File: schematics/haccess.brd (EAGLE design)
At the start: 86 x 86 mm, 34 parts, among them Q1 BSS123, SW1 SPST_TACT, SW2 SPST_TACT, U1 MCP2300X/SO, U2 ESP826607B, U3 OPTOISOLATOR-2SOIC8

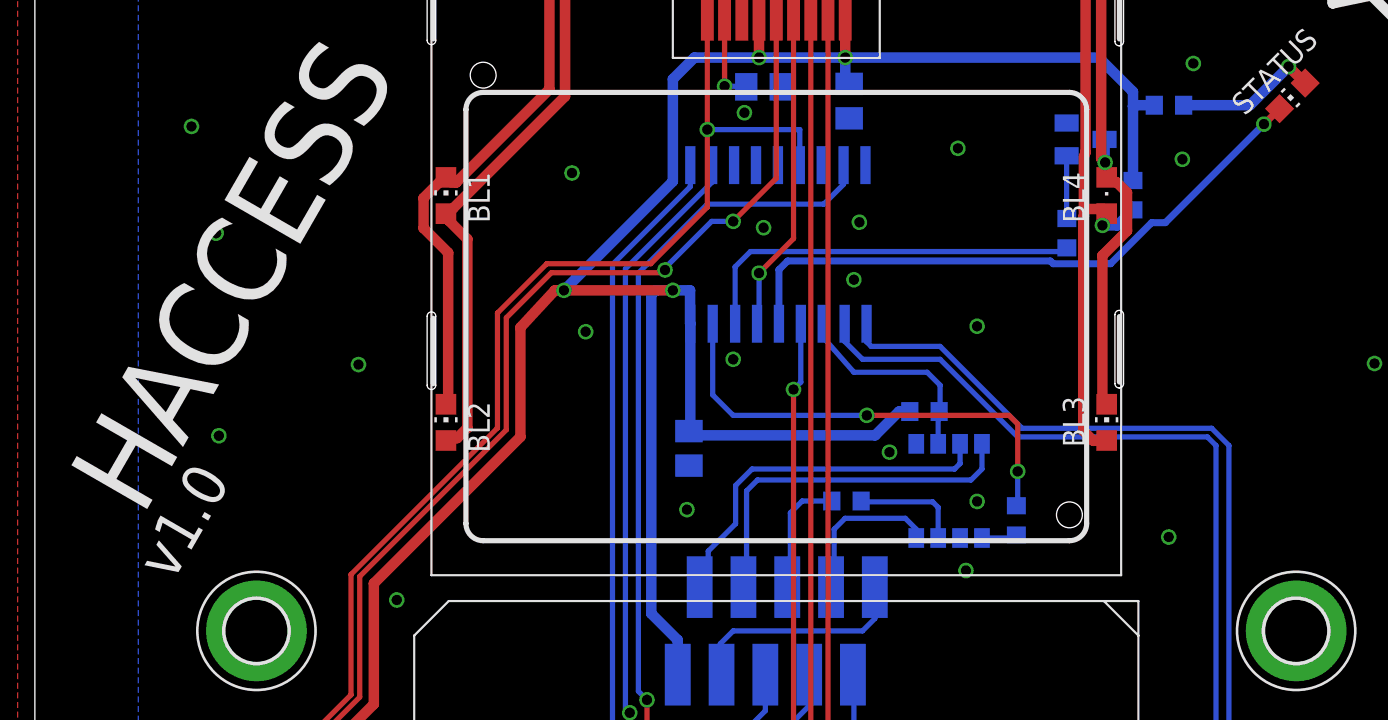
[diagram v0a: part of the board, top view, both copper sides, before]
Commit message: Increased status LED track sizes, changed 0805 leds to consistent package
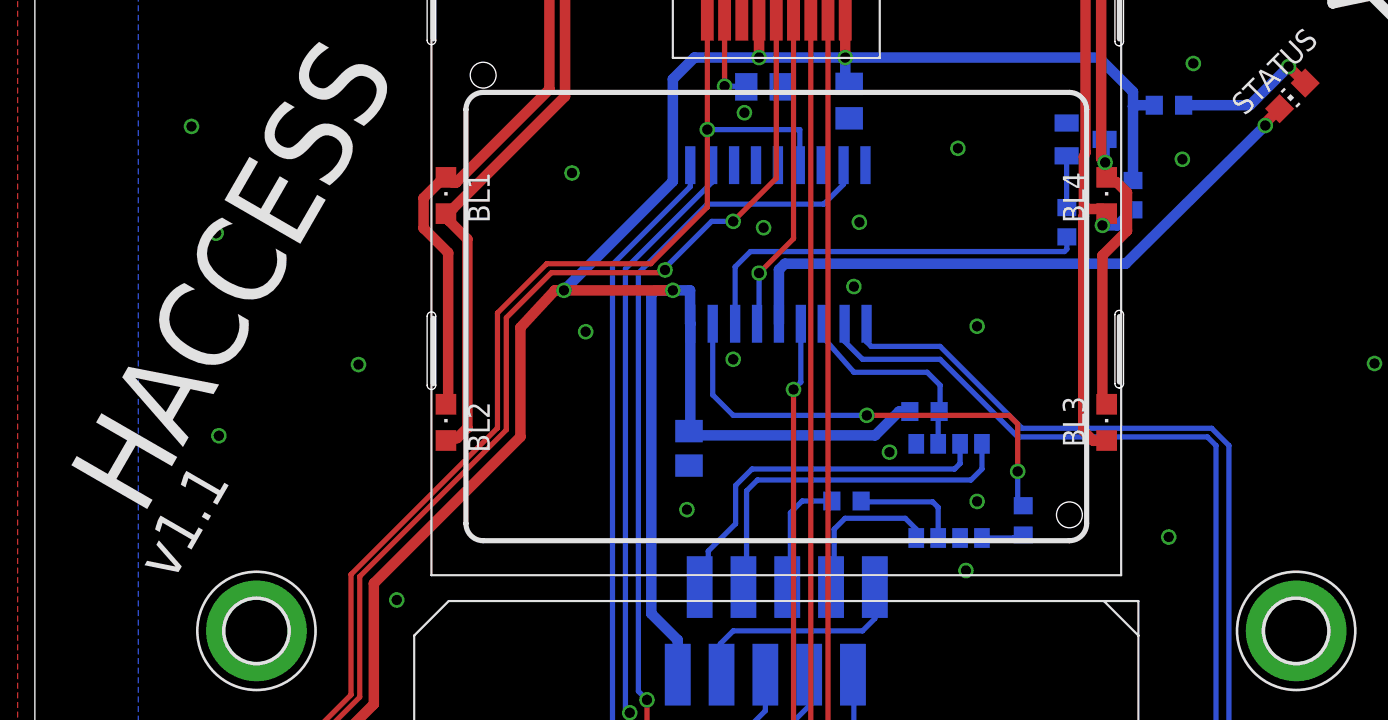
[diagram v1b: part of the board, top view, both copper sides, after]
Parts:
- BL1, BL2, BL3: device led:CHIP-LED0805 -> led:CHIPLED_0805
- moved R7 0.64 mm to (59.9, 66.7)
- moved R9 0.40 mm to (57.3, 49.4)
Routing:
- net OUT_LCD_BL: track 23.0 -> 23.7 mm
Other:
- board text added: "v1.1"
- board text removed: "v1.0"
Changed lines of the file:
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@@
 <text x="24.60625" y="7.77875" size="1.778" layer="122">+</text>
 <text x="11.43" y="63.65875" size="5.08" layer="121" rot="R60" align="center">HACCESS</text>
-<text x="8.5725" y="49.37125" size="2.54" layer="121" rot="R60" align="center">v1.0</text>
+<text x="8.5725" y="49.37125" size="2.54" layer="121" rot="R60" align="center">v1.1</text>
 <wire x1="75.276103125" y1="79.3942625" x2="79.76623125" y2="75.353146875" width="0.6096" layer="121" curve="-285.714585"/>
 <wire x1="79.76623125" y1="75.353146875" x2="80.664259375" y2="80.51679375" width="0.6096" layer="121"/>
@@
 <attribute name="NAME" x="49.36625" y="74.88375" size="1.016" layer="26" rot="MR270"/>
 </element>
-<element name="BL1" library="led" package="CHIP-LED0805" value="" x="23.84125" y="68.25" smashed="yes">
+<element name="BL1" library="led" package="CHIPLED_0805" value="" x="23.84125" y="68.25" smashed="yes">
 <attribute name="NAME" x="26.38125" y="66.6625" size="1.27" layer="25" rot="R90"/>
 <attribute name="VALUE" x="25.74625" y="66.98" size="1.27" layer="27" rot="R90"/>
@@
 <attribute name="NAME" x="64.63875" y="67.1575" size="1.27" layer="26" rot="MR90"/>
 </element>
-<element name="BL2" library="led" package="CHIP-LED0805" value="" x="23.84125" y="55.09125" smashed="yes">
+<element name="BL2" library="led" package="CHIPLED_0805" value="" x="23.84125" y="55.09125" smashed="yes">
 <attribute name="NAME" x="26.38125" y="53.345" size="1.27" layer="25" rot="R90"/>
 <attribute name="VALUE" x="25.74625" y="53.82125" size="1.27" layer="27" rot="R90"/>
 </element>
-<element name="BL3" library="led" package="CHIP-LED0805" value="" x="62.15875" y="55.09125" smashed="yes">
+<element name="BL3" library="led" package="CHIPLED_0805" value="" x="62.15875" y="55.09125" smashed="yes">
 <attribute name="NAME" x="60.88875" y="53.6625" size="1.27" layer="25" rot="R90"/>
 <attribute name="VALUE" x="64.06375" y="53.82125" size="1.27" layer="27" rot="R90"/>
@@
 <attribute name="NAME" x="62.16375" y="73.32" size="1.27" layer="26" rot="MR0"/>
 </element>
-<element name="R7" library="rcl" package="R0603" value="22R" x="59.85125" y="66.065" smashed="yes" rot="MR270">
-<attribute name="NAME" x="58.89875" y="67.17625" size="1.27" layer="26" rot="MR270"/>
+<element name="R7" library="rcl" package="R0603" value="22R" x="59.85125" y="66.7" smashed="yes" rot="MR270">
+<attribute name="NAME" x="58.89875" y="67.81125" size="1.27" layer="26" rot="MR270"/>
 </element>
 <element name="U1" library="adafruit" package="SO18W" value="MCP2300X/SO" x="42.4575" y="65.4125" smashed="yes" rot="MR180">
@@
 </element>
 <element name="U$1" library="PN532" package="SMALL-MODULE" value="PN532SMALLMODULE" x="64" y="44.73" rot="R180"/>
-<element name="R9" library="rcl" package="R0603" value="220R" x="56.9225" y="49.4075" smashed="yes" rot="MR90">
-<attribute name="NAME" x="57.71625" y="48.29625" size="1.27" layer="26" rot="MR90"/>
+<element name="R9" library="rcl" package="R0603" value="220R" x="57.319375" y="49.4075" smashed="yes" rot="MR90">
+<attribute name="NAME" x="57.875" y="47.105625" size="1.27" layer="26" rot="MR90"/>
 </element>
 <element name="R10" library="rcl" package="R0603" value="220R" x="47.07" y="50.5325" smashed="yes" rot="MR0">
@@
 <via x="20.51375" y="32.7275" extent="1-16" drill="0.6"/>
 <via x="47.81875" y="66.7" extent="1-16" drill="0.6"/>
-<via x="47.50125" y="63.36625" extent="1-16" drill="0.6"/>
+<via x="47.50125" y="62.969375" extent="1-16" drill="0.6"/>
 <via x="31.94375" y="60.35" extent="1-16" drill="0.6"/>
 <via x="54.645" y="50.5075" extent="1-16" drill="0.6"/>
@@
 <wire x1="40.6125" y1="60.8125" x2="40.6125" y2="64.1125" width="0.3048" layer="16"/>
 <wire x1="40.6125" y1="64.1125" x2="41.5" y2="65" width="0.3048" layer="16"/>
-<wire x1="41.5" y1="65" x2="59.63625" y2="65" width="0.3048" layer="16"/>
-<wire x1="59.63625" y1="65" x2="59.85125" y2="65.215" width="0.3048" layer="16"/>
+<wire x1="41.5" y1="65" x2="59.715625" y2="65" width="0.3048" layer="16"/>
+<wire x1="59.85125" y1="65.85" x2="59.85125" y2="65.135625" width="0.3048" layer="16"/>
+<wire x1="59.85125" y1="65.135625" x2="59.715625" y2="65" width="0.3048" layer="16"/>
 </signal>
 <signal name="N$22">
 <contactref element="Q1" pad="1"/>
 <contactref element="R7" pad="1"/>
-<wire x1="59.8375" y1="70.55375" x2="59.8375" y2="66.92875" width="0.3048" layer="16"/>
-<wire x1="59.8375" y1="66.92875" x2="59.85125" y2="66.915" width="0.3048" layer="16"/>
+<wire x1="59.8375" y1="70.55375" x2="59.8375" y2="67.405" width="0.3048" layer="16"/>
+<wire x1="59.8375" y1="67.405" x2="59.85125" y2="67.55" width="0.3048" layer="16"/>
 </signal>
 <signal name="SDA">
@@
 <wire x1="9.8425" y1="14.76375" x2="10.795" y2="14.76375" width="0.3048" layer="1"/>
 </signal>
-<signal name="OUT_STATUS_LED">
+<signal name="OUT_STATUS_LED" class="1">
 <contactref element="STATUS" pad="C"/>
 <contactref element="U1" pad="14"/>
-<wire x1="43.1525" y1="60.8125" x2="43.1525" y2="63.94875" width="0.4064" layer="16"/>
-<wire x1="43.1525" y1="63.94875" x2="43.65625" y2="64.4525" width="0.4064" layer="16"/>
-<wire x1="43.65625" y1="64.4525" x2="58.89625" y2="64.4525" width="0.4064" layer="16"/>
-<wire x1="58.89625" y1="64.4525" x2="59.055" y2="64.29375" width="0.4064" layer="16"/>
-<wire x1="59.055" y1="64.29375" x2="62.38875" y2="64.29375" width="0.4064" layer="16"/>
-<wire x1="62.38875" y1="64.29375" x2="64.77" y2="66.675" width="0.4064" layer="16"/>
-<wire x1="64.77" y1="66.675" x2="65.56375" y2="66.675" width="0.4064" layer="16"/>
-<wire x1="65.56375" y1="66.675" x2="71.27875" y2="72.39" width="0.4064" layer="16"/>
-<via x="71.27875" y="72.39" extent="1-16" drill="0.6"/>
-<wire x1="71.27875" y1="72.39" x2="71.293984375" y2="72.39" width="0.4064" layer="1"/>
-<wire x1="71.293984375" y1="72.39" x2="72.188146875" y2="73.2841625" width="0.4064" layer="1"/>
+<wire x1="43.1525" y1="60.8125" x2="43.1525" y2="63.94875" width="0.6096" layer="16"/>
+<wire x1="43.1525" y1="63.94875" x2="43.4975" y2="64.29375" width="0.6096" layer="16"/>
+<wire x1="43.4975" y1="64.29375" x2="63.261875" y2="64.29375" width="0.6096" layer="16"/>
+<wire x1="63.261875" y1="64.29375" x2="71.358125" y2="72.310625" width="0.6096" layer="16"/>
+<via x="71.358125" y="72.310625" extent="1-16" drill="0.6"/>
+<wire x1="71.358125" y1="72.310625" x2="71.293984375" y2="72.39" width="0.6096" layer="1"/>
+<wire x1="71.293984375" y1="72.39" x2="72.188146875" y2="73.2841625" width="0.6096" layer="1"/>
 </signal>
 <signal name="OUT_OPTO">
@@
 <via x="57" y="52.25" extent="1-16" drill="0.6"/>
 <wire x1="57" y1="52.25" x2="57" y2="50.335" width="0.3048" layer="16"/>
-<wire x1="57" y1="50.335" x2="56.9225" y2="50.2575" width="0.3048" layer="16"/>
+<wire x1="57" y1="50.335" x2="57.319375" y2="50.2575" width="0.3048" layer="16"/>
 </signal>
 <signal name="ADC">
@@
 <wire x1="46.355" y1="45.72" x2="46.175" y2="45.54" width="0.3048" layer="16"/>
 </signal>
-<signal name="N$2">
+<signal name="N$2" class="1">
 <contactref element="STATUS" pad="A"/>
 <contactref element="R12" pad="2"/>
@@
 <contactref element="R9" pad="1"/>
 <wire x1="54.9275" y1="48.387" x2="56.752" y2="48.387" width="0.3048" layer="16"/>
-<wire x1="56.752" y1="48.387" x2="56.9225" y2="48.5575" width="0.3048" layer="16"/>
+<wire x1="56.752" y1="48.387" x2="57.319375" y2="48.5575" width="0.3048" layer="16"/>
 </signal>
 <signal name="N$4">

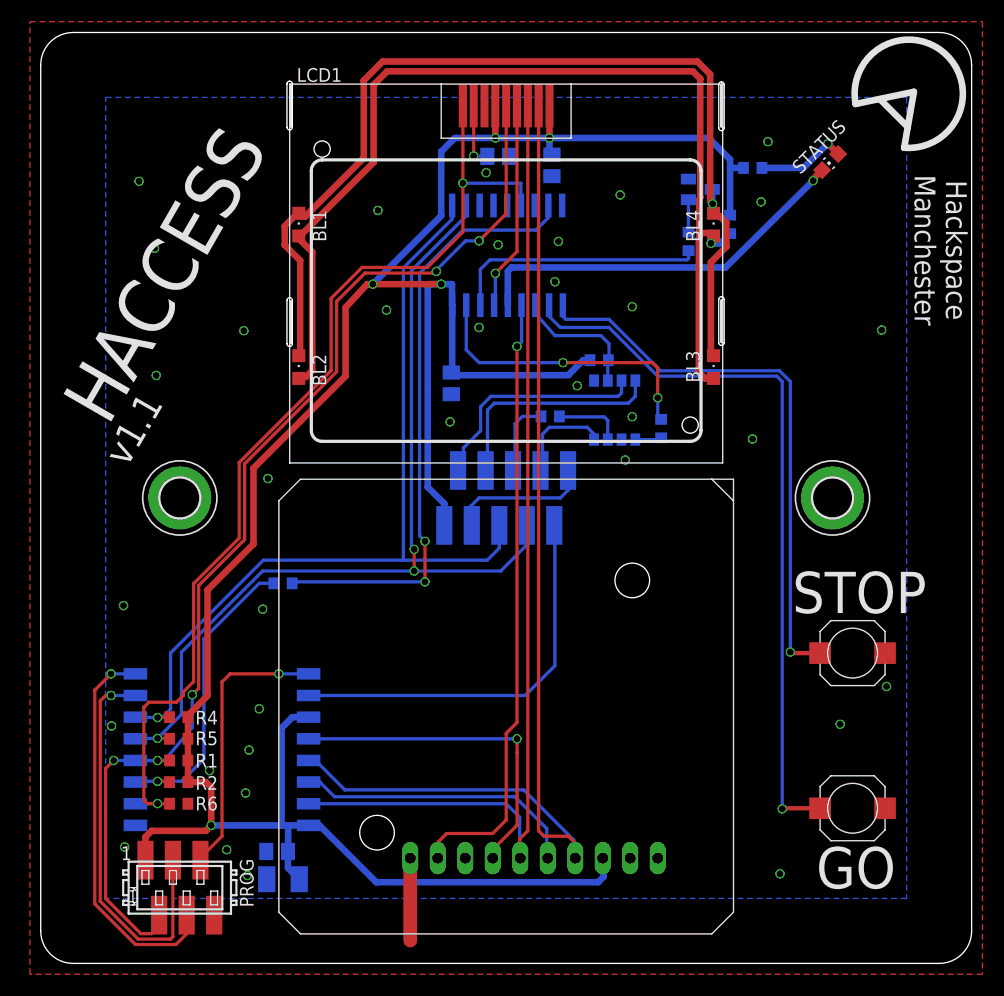
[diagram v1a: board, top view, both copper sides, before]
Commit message: Increased aerial keepout, routing tweaks
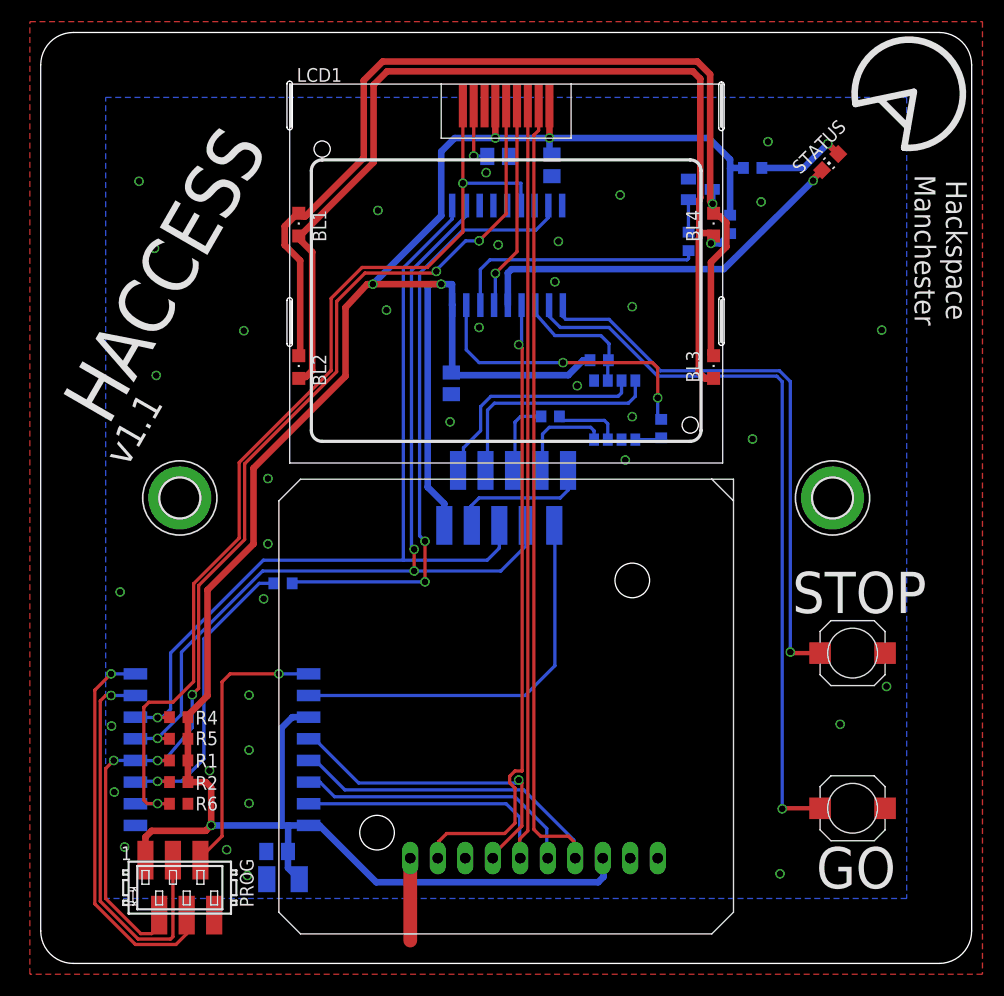
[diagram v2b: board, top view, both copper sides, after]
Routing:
- net IN_532_IRQ: track 56.8 -> 58.5 mm
- net CS1: track 31.2 -> 29.8 mm
- net SCK: track 101.5 -> 102.0 mm
- net GND: vias 35 -> 37
